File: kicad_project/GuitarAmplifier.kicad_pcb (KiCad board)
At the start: 4 copper layers, 158.5 x 57 mm, 41 parts, among them J1 NMJ6HCD2, J2 Screw_Terminal_01x02, J3 Screw_Terminal_01x02, J4 Terminal_01x03, U1 TL072CP, U2 TL072CP, U3 LM386

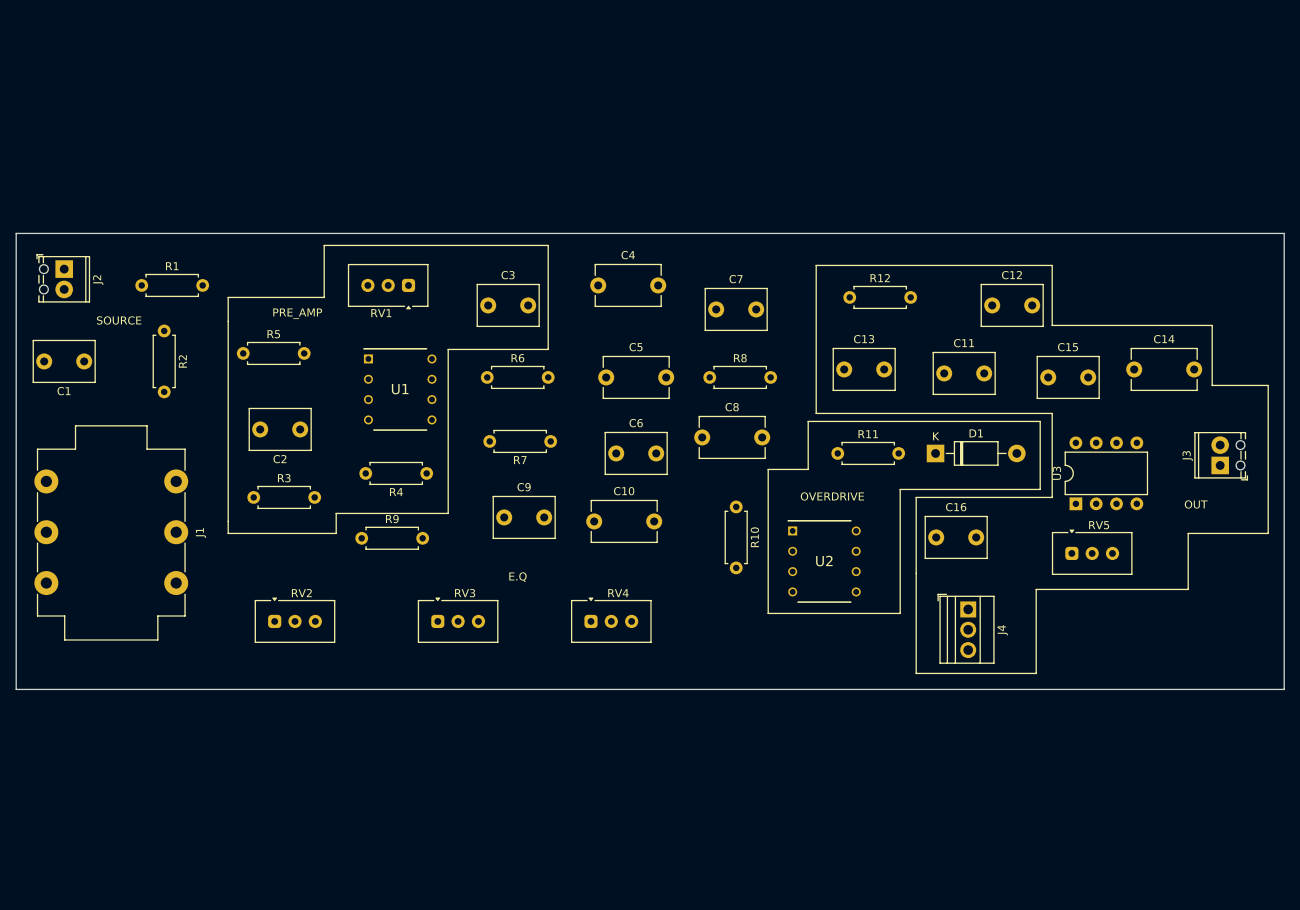
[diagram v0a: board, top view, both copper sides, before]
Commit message: Realizando acomodo final en el esquematico y PCB
Signed-off-by: RoMadrigal <rmadrigalmontes@gmail.com>
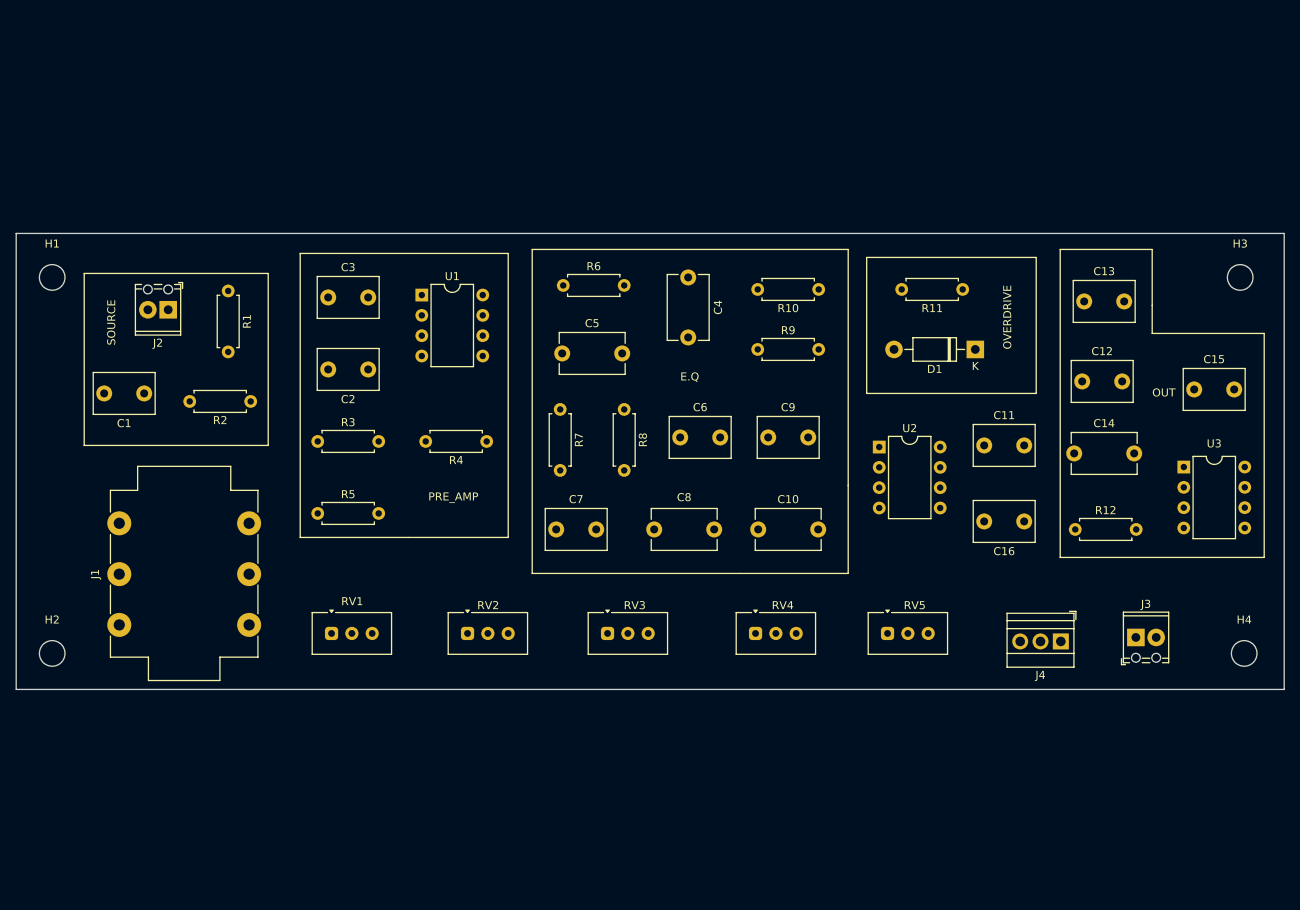
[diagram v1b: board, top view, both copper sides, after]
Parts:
- added H1: MountingHole_3.2mm_M3, MountingHole:MountingHole_3.2mm_M3, F.Cu at (105.0, 118.0)
- added H2: MountingHole_3.2mm_M3, MountingHole:MountingHole_3.2mm_M3, F.Cu at (105.0, 165.0)
- added H3: MountingHole_3.2mm_M3, MountingHole:MountingHole_3.2mm_M3, F.Cu at (253.5, 118.0)
- added H4: MountingHole_3.2mm_M3, MountingHole:MountingHole_3.2mm_M3, F.Cu at (254.0, 165.0)
- R12: value 10k -> 10
- U1, U2: footprint Huella:TL072Cp -> Package_DIP:DIP-8_W7.62mm
- moved R9 54.8 mm to (193.2, 127.0)
- moved RV1 44.6 mm to (139.9, 162.5), turned to 0 degrees
- moved R12 40.4 mm to (232.9, 149.5)
- moved C9 34.5 mm to (194.5, 138.0)
- moved C7 34.0 mm to (168.0, 149.5)
- moved C13 31.2 mm to (234.0, 121.0)
- moved R10 29.1 mm to (200.8, 119.5), turned to 180 degrees
- moved R11 25.8 mm to (218.8, 119.5), turned to 180 degrees
- moved RV5 25.1 mm to (209.4, 162.5)
- moved RV2 24.2 mm to (156.9, 162.5)
- moved J3 23.9 mm to (240.5, 163.0), turned to 0 degrees
- moved R5 22.1 mm to (138.2, 147.5)
- moved RV3 21.3 mm to (174.4, 162.5)
- moved RV4 20.6 mm to (192.9, 162.5)
- moved C10 20.5 mm to (193.2, 149.5)
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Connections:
- J3 pad 1: unconnected-(J3-Pin_1-Pad1) -> GND
- J4 pad 3: /OUT_Eq -> /OUT_Clean
- R10 pad 1: Net-(U2-1OUT) -> /OUT_Clean
- U2 pad 1: Net-(U2-1OUT) -> /OUT_Clean
- U2 pad 5: /OUT_Eq -> /OUT_Clean
- U3 pad 1: GND -> unconnected-(U3-GAIN-Pad1)
- U3 pad 8: GND -> unconnected-(U3-GAIN-Pad8)

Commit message: Definiendo las capas de alimentacion y tierra en la PCB
Signed-off-by: RoMadrigal <rmadrigalmontes@gmail.com>
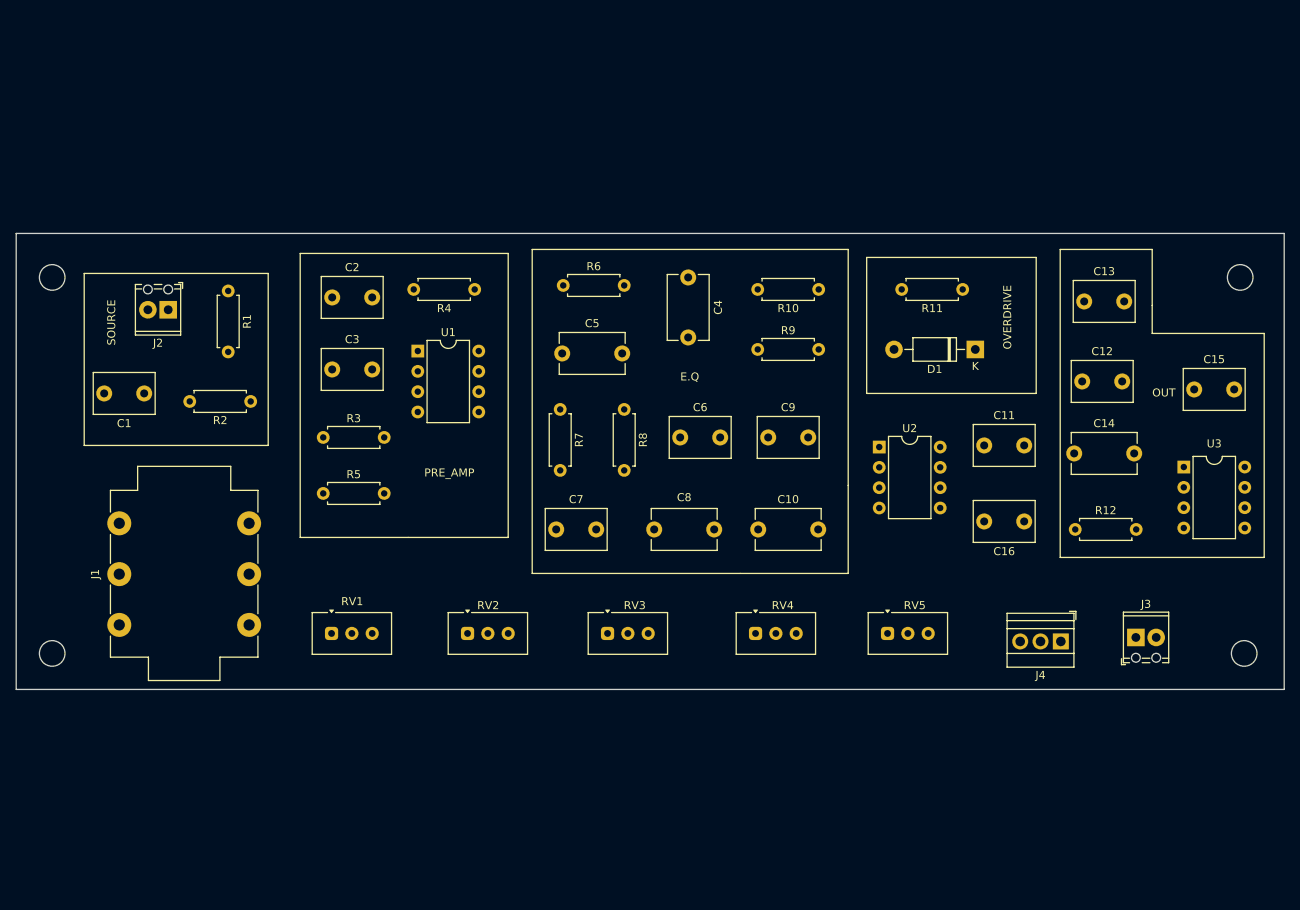
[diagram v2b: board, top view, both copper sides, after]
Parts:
- moved R4 19.1 mm to (157.8, 119.5)
- moved C2 10.1 mm to (140.0, 120.5), turned to 0 degrees
- moved C3 9.01 mm to (140.0, 129.5)
- moved U1 7.02 mm to (150.7, 127.2)
- moved R5 2.59 mm to (138.9, 145.0)
- moved R3 0.85 mm to (138.9, 138.0)
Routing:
- added copper zone on In1.Cu, net +4.5V
- added copper zone on In1.Cu, net +9V
- added copper zone on In2.Cu, net GND
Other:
- board text added: "+4.5V"
- board text added: "+9V"
- board text added: "GND"
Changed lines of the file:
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@@
 	(footprint "Resistor_THT:R_Axial_DIN0207_L6.3mm_D2.5mm_P7.62mm_Horizontal"
 		(layer "F.Cu")
-		(at 138.19 147.5)
+		(at 138.88 145)
 		(descr "Resistor, Axial_DIN0207 series, Axial, Horizontal, pin pitch=7.62mm, 0.25W = 1/4W, length*diameter=6.3*2.5mm^2, http://cdn-reichelt.de/documents/datenblatt/B400/1_4W%23YAG.pdf")
 		(tags "Resistor Axial_DIN0207 series Axial Horizontal pin pitch 7.62mm 0.25W = 1/4W length 6.3mm diameter 2.5mm")
@@
 			(at 0 -4.2 0)
 			(layer "F.SilkS")
+			(hide yes)
 			(effects
 				(font
@@
 	(footprint "Resistor_THT:R_Axial_DIN0207_L6.3mm_D2.5mm_P7.62mm_Horizontal"
 		(layer "F.Cu")
-		(at 159.31 138.5 180)
+		(at 157.81 119.5 180)
 		(descr "Resistor, Axial_DIN0207 series, Axial, Horizontal, pin pitch=7.62mm, 0.25W = 1/4W, length*diameter=6.3*2.5mm^2, http://cdn-reichelt.de/documents/datenblatt/B400/1_4W%23YAG.pdf")
 		(tags "Resistor Axial_DIN0207 series Axial Horizontal pin pitch 7.62mm 0.25W = 1/4W length 6.3mm diameter 2.5mm")
@@
 			(at 0 -4.2 0)
 			(layer "F.SilkS")
+			(hide yes)
 			(effects
 				(font
@@
 	(footprint "Capacitor_THT:C_Disc_D7.5mm_W5.0mm_P5.00mm"
 		(layer "F.Cu")
-		(at 139.5 120.5)
+		(at 140 129.5)
 		(descr "C, Disc series, Radial, pin pitch=5.00mm, , diameter*width=7.5*5.0mm^2, Capacitor, http://www.vishay.com/docs/28535/vy2series.pdf")
 		(tags "C Disc series Radial pin pitch 5.00mm  diameter 7.5mm width 5.0mm Capacitor")
@@
 			(at 0 -4.2 0)
 			(layer "F.SilkS")
+			(hide yes)
 			(effects
 				(font
@@
 	(footprint "Capacitor_THT:C_Disc_D7.5mm_W5.0mm_P5.00mm"
 		(layer "F.Cu")
-		(at 144.5 129.5 180)
+		(at 140 120.5)
 		(descr "C, Disc series, Radial, pin pitch=5.00mm, , diameter*width=7.5*5.0mm^2, Capacitor, http://www.vishay.com/docs/28535/vy2series.pdf")
 		(tags "C Disc series Radial pin pitch 5.00mm  diameter 7.5mm width 5.0mm Capacitor")
@@
 		)
 		(property "Footprint" "Capacitor_THT:C_Disc_D7.5mm_W5.0mm_P5.00mm"
-			(at 0 0 180)
+			(at 0 0 0)
 			(unlocked yes)
 			(layer "F.Fab")
@@
 		)
 		(property "Datasheet" ""
-			(at 0 0 180)
+			(at 0 0 0)
 			(unlocked yes)
 			(layer "F.Fab")
@@
 		)
 		(property "Description" "Unpolarized capacitor"
-			(at 0 0 180)
+			(at 0 0 0)
 			(unlocked yes)
 			(layer "F.Fab")
@@
 		(attr through_hole)
 		(fp_line
-			(start 6.37 -2.62)
-			(end 6.37 2.62)
+			(start -1.37 -2.62)
+			(end -1.37 2.62)
 			(stroke
 				(width 0.12)
@@
 		)
 		(fp_line
-			(start -1.37 2.62)
-			(end 6.37 2.62)
+			(start -1.37 -2.62)
+			(end 6.37 -2.62)
 			(stroke
 				(width 0.12)
@@
 		)
 		(fp_line
-			(start -1.37 -2.62)
-			(end 6.37 -2.62)
+			(start -1.37 2.62)
+			(end 6.37 2.62)
 			(stroke
 				(width 0.12)
@@
 		)
 		(fp_line
-			(start -1.37 -2.62)
-			(end -1.37 2.62)
+			(start 6.37 -2.62)
+			(end 6.37 2.62)
 			(stroke
 				(width 0.12)
@@
 		)
 		(fp_line
-			(start 6.5 2.75)
-			(end 6.5 -2.75)
+			(start -1.5 -2.75)
+			(end -1.5 2.75)
 			(stroke
 				(width 0.05)
@@
 		)
 		(fp_line
-			(start 6.5 -2.75)
-			(end -1.5 -2.75)
+			(start -1.5 2.75)
+			(end 6.5 2.75)
 			(stroke
 				(width 0.05)
@@
 		)
 		(fp_line
-			(start -1.5 2.75)
-			(end 6.5 2.75)
+			(start 6.5 -2.75)
+			(end -1.5 -2.75)
 			(stroke
 				(width 0.05)
@@
 		)
 		(fp_line
-			(start -1.5 -2.75)
-			(end -1.5 2.75)
+			(start 6.5 2.75)
+			(end 6.5 -2.75)
 			(stroke
 				(width 0.05)
@@
 		)
 		(fp_line
-			(start 6.25 2.5)
-			(end 6.25 -2.5)
+			(start -1.25 -2.5)
+			(end -1.25 2.5)
 			(stroke
 				(width 0.1)
@@
 		)
 		(fp_line
-			(start 6.25 -2.5)
-			(end -1.25 -2.5)
+			(start -1.25 2.5)
+			(end 6.25 2.5)
 			(stroke
 				(width 0.1)
@@
 		)
 		(fp_line
-			(start -1.25 2.5)
-			(end 6.25 2.5)
+			(start 6.25 -2.5)
+			(end -1.25 -2.5)
 			(stroke
 				(width 0.1)
@@
 		)
 		(fp_line
-			(start -1.25 -2.5)
-			(end -1.25 2.5)
+			(start 6.25 2.5)
+			(end 6.25 -2.5)
 			(stroke
 				(width 0.1)
@@
 		)
 		(pad "1" thru_hole circle
-			(at 0 0 180)
+			(at 0 0)
 			(size 2 2)
 			(drill 1)
@@
 		)
 		(pad "2" thru_hole circle
-			(at 5 0 180)
+			(at 5 0)
 			(size 2 2)
 			(drill 1)
@@
 	(footprint "Resistor_THT:R_Axial_DIN0207_L6.3mm_D2.5mm_P7.62mm_Horizontal"
 		(layer "F.Cu")
-		(at 138.19 138.5)
+		(at 138.88 138)
 		(descr "Resistor, Axial_DIN0207 series, Axial, Horizontal, pin pitch=7.62mm, 0.25W = 1/4W, length*diameter=6.3*2.5mm^2, http://cdn-reichelt.de/documents/datenblatt/B400/1_4W%23YAG.pdf")
 		(tags "Resistor Axial_DIN0207 series Axial Horizontal pin pitch 7.62mm 0.25W = 1/4W length 6.3mm diameter 2.5mm")
@@
 			(at 0 -4.2 0)
 			(layer "F.SilkS")
+			(hide yes)
 			(effects
 				(font
@@
 	(footprint "Package_DIP:DIP-8_W7.62mm"
 		(layer "F.Cu")
-		(at 151.2 120.2)
+		(at 150.7 127.2)
 		(descr "8-lead though-hole mounted DIP package, row spacing 7.62 mm (300 mils)")
 		(tags "THT DIP DIL PDIP 2.54mm 7.62mm 300mil")
@@
 		(layer "Edge.Cuts")
 	)
+	(gr_text "+4.5V"
+		(at 102.5 143.5 0)
+		(layer "In1.Cu")
+		(effects
+			(font
+				(size 1.5 1.5)
+				(thickness 0.3)
+				(bold yes)
+			)
+			(justify left bottom)
+		)
+	)
+	(gr_text "+9V"
+		(at 114 116.5 0)
+		(layer "In1.Cu")
+		(effects
+			(font
+				(size 1.5 1.5)
+				(thickness 0.3)
+				(bold yes)
+			)
+			(justify left bottom)
+		)
+	)
+	(gr_text "GND"
+		(at 102.5 158.5 0)
+		(layer "In2.Cu")
+		(effects
+			(font
+				(size 1.5 1.5)
+				(thickness 0.3)
+				(bold yes)
+			)
+			(justify left bottom)
+		)
+	)
 	(gr_text "E.Q"
 		(at 183.5 131 0)
@@
 	)
 	(gr_text "PRE_AMP"
-		(at 152 146 0)
+		(at 151.5 143 0)
 		(layer "F.SilkS")
 		(effects
@@
 		)
 	)
+	(zone
+		(net 1)
+		(net_name "+4.5V")
+		(layer "In1.Cu")
+		(hatch edge 0.5)
+		(priority 1)
+		(connect_pads
+			(clearance 0.5)
+		)
+		(min_thickness 0.25)
+		(filled_areas_thickness no)
+		(fill yes
+			(thermal_gap 0.5)
+			(thermal_bridge_width 0.5)
+		)
+		(polygon
+			(pts
+				(xy 100.5 126) (xy 137.5 126) (xy 137.5 134.5) (xy 149 134.5) (xy 149 143) (xy 218.5 143) (xy 218.5 154)
+				(xy 259 154) (xy 259 169.5) (xy 100.5 169.5)
+			)
+		)
+	)
+	(zone
+		(net 4)
+		(net_name "+9V")
+		(layer "In1.Cu")
+		(hatch edge 0.5)
+		(connect_pads
+			(clearance 0.5)
+		)
+		(min_thickness 0.25)
+		(filled_areas_thickness no)
+		(fill yes
+			(thermal_gap 0.5)
+			(thermal_bridge_width 0.5)
+		)
+		(polygon
+			(pts
+				(xy 100.5 112.5) (xy 100.5 126) (xy 137.5 126) (xy 137.5 134.5) (xy 149 134.5) (xy 149 143) (xy 218.5 143)
+				(xy 218.5 154) (xy 259 154) (xy 259 112.5)
+			)
+		)
+	)
+	(zone
+		(net 2)
+		(net_name "GND")
+		(layer "In2.Cu")
+		(hatch edge 0.5)
+		(priority 2)
+		(connect_pads
+			(clearance 0.5)
+		)
+		(min_thickness 0.25)
+		(filled_areas_thickness no)
+		(fill yes
+			(thermal_gap 0.5)
+			(thermal_bridge_width 0.5)
+		)
+		(polygon
+			(pts
+				(xy 100.5 112.5) (xy 100.5 169.5) (xy 259 169.5) (xy 259 112.5)
+			)
+		)
+	)

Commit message: Conectando pistas y vias en la capa superior de la PCB
Signed-off-by: RoMadrigal <rmadrigalmontes@gmail.com>
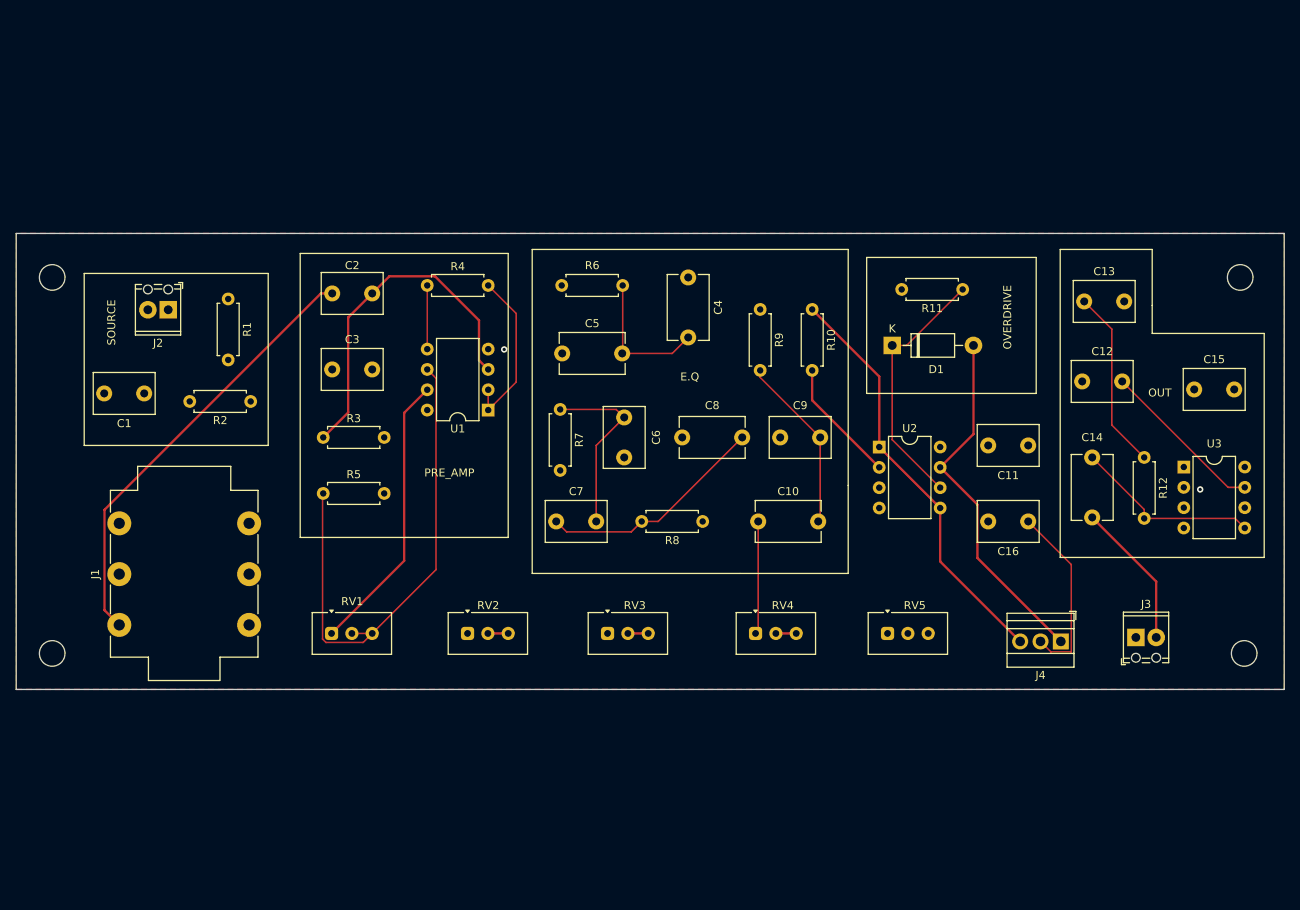
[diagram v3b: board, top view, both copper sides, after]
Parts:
- moved R8 17.1 mm to (186.3, 148.5), turned to 180 degrees
- moved R12 12.5 mm to (241.5, 140.5), turned to -90 degrees
- moved C8 12.0 mm to (183.8, 138.0)
- moved U1 11.5 mm to (159.5, 134.6), turned to 180 degrees
- moved D1 10.4 mm to (210.0, 126.5), turned to 0 degrees
- moved C6 7.43 mm to (176.5, 140.5), turned to 90 degrees
- moved R6 7.43 mm to (176.3, 119.0), turned to 180 degrees
- moved C9 6.50 mm to (201.0, 138.0), turned to 180 degrees
- moved R4 5.95 mm to (151.9, 119.0), turned to 0 degrees
- moved C11 5.50 mm to (227.0, 139.0), turned to 180 degrees
- moved C2 5.02 mm to (145.0, 120.0), turned to 180 degrees
- moved R9 5.01 mm to (193.5, 122.0), turned to -90 degrees
- moved R10 2.63 mm to (200.0, 122.0), turned to -90 degrees
- moved C14 2.30 mm to (235.0, 140.5), turned to -90 degrees
- moved C10 1.00 mm to (193.2, 148.5)
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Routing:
- net Net-(U1-2IN-): track 0.00 -> 64.4 mm
- net Net-(C2-Pad2): track 0.00 -> 55.2 mm
- net /OUT_Clean: track 0.00 -> 52.3 mm
- net /OUT_OverD: track 0.00 -> 45.0 mm
- net Net-(U1-1IN+): track 0.00 -> 43.7 mm
- net /OUT_PreAmp: track 0.00 -> 35.4 mm
- net Net-(D1-K): track 0.00 -> 32.0 mm
- net Net-(C7-Pad1): track 0.00 -> 28.7 mm
- net Net-(C14-Pad1): track 0.00 -> 23.4 mm
- net /OUT_Eq: track 0.00 -> 23.2 mm
- net Net-(J4-Pin_2): track 0.00 -> 22.9 mm
- net Net-(C6-Pad2): track 0.00 -> 22.9 mm
- net Net-(C13-Pad1): track 0.00 -> 22.6 mm
- net Net-(C10-Pad2): track 0.00 -> 22.1 mm
- net Net-(U1-1IN-): track 0.00 -> 21.0 mm
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- added copper zone on F.Cu, net GND
